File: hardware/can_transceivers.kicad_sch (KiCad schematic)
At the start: 0 parts

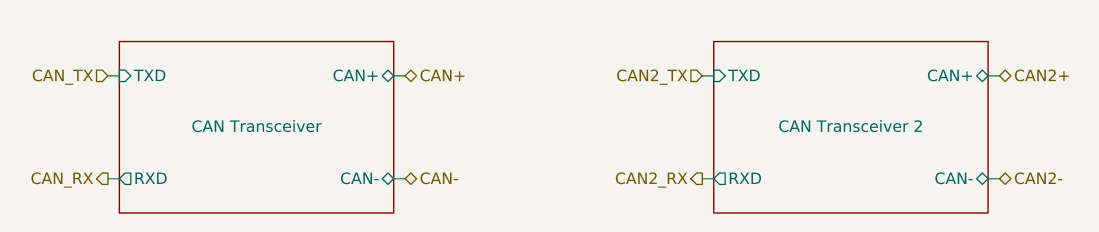
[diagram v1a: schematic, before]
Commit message: Improve the diagram based on the feedback
- add an input LC filter
- remove the USB connector
- add a programmer connector
- move optocouplers into a subsheet
- add a suspension tension meter IC
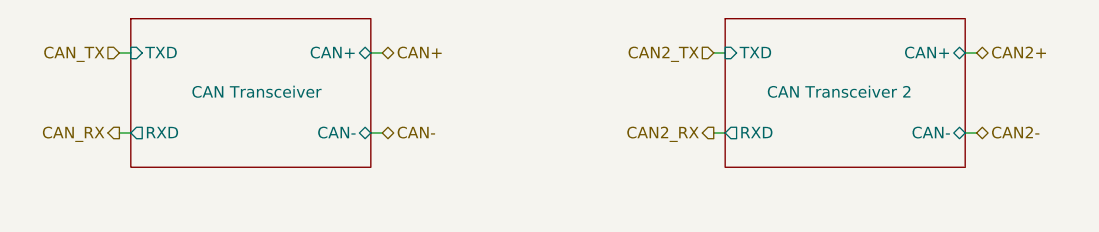
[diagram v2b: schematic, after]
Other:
- title: (none) -> CAN Transceivers
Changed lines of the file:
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@@
   (paper "A4")
   (title_block
-    (date "2023-09-20")
+    (title "CAN Transceivers")
+    (date "2023-10-01")
     (rev "${REVISION}")
     (company "Author: I. Kajdan")
     (comment 1 "Reviewer:")
   )
-  (wire (pts (xy 132.08 106.68) (xy 133.35 106.68))
+  (wire (pts (xy 129.54 101.6) (xy 130.81 101.6))
     (stroke (width 0) (type default))
   )
-  (wire (pts (xy 100.33 106.68) (xy 101.6 106.68))
+  (wire (pts (xy 101.6 101.6) (xy 102.87 101.6))
     (stroke (width 0) (type default))
   )
-  (wire (pts (xy 166.37 95.25) (xy 167.64 95.25))
+  (wire (pts (xy 167.64 92.71) (xy 168.91 92.71))
     (stroke (width 0) (type default))
   )
-  (wire (pts (xy 132.08 95.25) (xy 133.35 95.25))
+  (wire (pts (xy 129.54 92.71) (xy 130.81 92.71))
     (stroke (width 0) (type default))
   )
-  (wire (pts (xy 166.37 106.68) (xy 167.64 106.68))
+  (wire (pts (xy 167.64 101.6) (xy 168.91 101.6))
     (stroke (width 0) (type default))
   )
-  (wire (pts (xy 100.33 95.25) (xy 101.6 95.25))
+  (wire (pts (xy 101.6 92.71) (xy 102.87 92.71))
     (stroke (width 0) (type default))
   )
-  (wire (pts (xy 198.12 95.25) (xy 199.39 95.25))
+  (wire (pts (xy 195.58 92.71) (xy 196.85 92.71))
     (stroke (width 0) (type default))
   )
-  (wire (pts (xy 198.12 106.68) (xy 199.39 106.68))
+  (wire (pts (xy 195.58 101.6) (xy 196.85 101.6))
     (stroke (width 0) (type default))
   )
-  (hierarchical_label "CAN2_RX" (shape output) (at 166.37 106.68 180) (fields_autoplaced)
+  (hierarchical_label "CAN2_RX" (shape output) (at 167.64 101.6 180) (fields_autoplaced)
     (effects (font (size 1.27 1.27)) (justify right))
   )
-  (hierarchical_label "CAN2+" (shape bidirectional) (at 199.39 95.25 0) (fields_autoplaced)
+  (hierarchical_label "CAN2+" (shape bidirectional) (at 196.85 92.71 0) (fields_autoplaced)
     (effects (font (size 1.27 1.27)) (justify left))
   )
-  (hierarchical_label "CAN-" (shape bidirectional) (at 133.35 106.68 0) (fields_autoplaced)
+  (hierarchical_label "CAN-" (shape bidirectional) (at 130.81 101.6 0) (fields_autoplaced)
     (effects (font (size 1.27 1.27)) (justify left))
   )
-  (hierarchical_label "CAN2-" (shape bidirectional) (at 199.39 106.68 0) (fields_autoplaced)
+  (hierarchical_label "CAN2-" (shape bidirectional) (at 196.85 101.6 0) (fields_autoplaced)
     (effects (font (size 1.27 1.27)) (justify left))
   )
-  (hierarchical_label "CAN_RX" (shape output) (at 100.33 106.68 180) (fields_autoplaced)
+  (hierarchical_label "CAN_RX" (shape output) (at 101.6 101.6 180) (fields_autoplaced)
     (effects (font (size 1.27 1.27)) (justify right))
   )
-  (hierarchical_label "CAN2_TX" (shape input) (at 166.37 95.25 180) (fields_autoplaced)
+  (hierarchical_label "CAN2_TX" (shape input) (at 167.64 92.71 180) (fields_autoplaced)
     (effects (font (size 1.27 1.27)) (justify right))
   )
-  (hierarchical_label "CAN_TX" (shape input) (at 100.33 95.25 180) (fields_autoplaced)
+  (hierarchical_label "CAN_TX" (shape input) (at 101.6 92.71 180) (fields_autoplaced)
     (effects (font (size 1.27 1.27)) (justify right))
   )
-  (hierarchical_label "CAN+" (shape bidirectional) (at 133.35 95.25 0) (fields_autoplaced)
+  (hierarchical_label "CAN+" (shape bidirectional) (at 130.81 92.71 0) (fields_autoplaced)
     (effects (font (size 1.27 1.27)) (justify left))
   )
-  (sheet (at 101.6 91.44) (size 30.48 19.05)
+  (sheet (at 102.87 88.9) (size 26.67 16.51)
     (stroke (width 0.1524) (type solid))
     (fill (color 0 0 0 0.0000))
-    (property "Sheetname" "CAN Transceiver" (at 116.84 100.8884 0)
+    (property "Sheetname" "CAN Transceiver" (at 116.84 97.0784 0)
       (effects (font (size 1.27 1.27)))
     )
-    (property "Sheetfile" "can_transceiver.kicad_sch" (at 101.6 108.5346 0)
+    (property "Sheetfile" "can_transceiver.kicad_sch" (at 102.87 105.9946 0)
       (effects (font (size 1.27 1.27)) (justify left top) hide)
     )
-    (pin "RXD" output (at 101.6 106.68 180)
+    (pin "RXD" output (at 102.87 101.6 180)
       (effects (font (size 1.27 1.27)) (justify left))
     )
-    (pin "TXD" input (at 101.6 95.25 180)
+    (pin "TXD" input (at 102.87 92.71 180)
       (effects (font (size 1.27 1.27)) (justify left))
     )
-    (pin "CAN-" bidirectional (at 132.08 106.68 0)
+    (pin "CAN-" bidirectional (at 129.54 101.6 0)
       (effects (font (size 1.27 1.27)) (justify right))
     )
-    (pin "CAN+" bidirectional (at 132.08 95.25 0)
+    (pin "CAN+" bidirectional (at 129.54 92.71 0)
       (effects (font (size 1.27 1.27)) (justify right))
     )
@@
       (project "rearbox"
         (path "/b652b05a-4e3d-4ad1-b032-18886abe7d45" (page "8"))
-        (path "/b652b05a-4e3d-4ad1-b032-18886abe7d45/38408e41-dfb1-4c27-acb0-3f1224cc8789" (page "6"))
+        (path "/b652b05a-4e3d-4ad1-b032-18886abe7d45/38408e41-dfb1-4c27-acb0-3f1224cc8789" (page "5"))
       )
     )
   )
-  (sheet (at 167.64 91.44) (size 30.48 19.05)
+  (sheet (at 168.91 88.9) (size 26.67 16.51)
     (stroke (width 0.1524) (type solid))
     (fill (color 0 0 0 0.0000))
-    (property "Sheetname" "CAN Transceiver 2" (at 182.88 100.8884 0)
+    (property "Sheetname" "CAN Transceiver 2" (at 181.61 97.0784 0)
       (effects (font (size 1.27 1.27)))
     )
-    (property "Sheetfile" "can_transceiver.kicad_sch" (at 167.64 108.5346 0)
+    (property "Sheetfile" "can_transceiver.kicad_sch" (at 168.91 105.9946 0)
       (effects (font (size 1.27 1.27)) (justify left top) hide)
     )
-    (pin "RXD" output (at 167.64 106.68 180)
+    (pin "RXD" output (at 168.91 101.6 180)
       (effects (font (size 1.27 1.27)) (justify left))
     )
-    (pin "TXD" input (at 167.64 95.25 180)
+    (pin "TXD" input (at 168.91 92.71 180)
       (effects (font (size 1.27 1.27)) (justify left))
     )
-    (pin "CAN-" bidirectional (at 198.12 106.68 0)
+    (pin "CAN-" bidirectional (at 195.58 101.6 0)
       (effects (font (size 1.27 1.27)) (justify right))
     )
-    (pin "CAN+" bidirectional (at 198.12 95.25 0)
+    (pin "CAN+" bidirectional (at 195.58 92.71 0)
       (effects (font (size 1.27 1.27)) (justify right))
     )
@@
       (project "rearbox"
         (path "/b652b05a-4e3d-4ad1-b032-18886abe7d45" (page "9"))
-        (path "/b652b05a-4e3d-4ad1-b032-18886abe7d45/38408e41-dfb1-4c27-acb0-3f1224cc8789" (page "7"))
+        (path "/b652b05a-4e3d-4ad1-b032-18886abe7d45/38408e41-dfb1-4c27-acb0-3f1224cc8789" (page "6"))
       )
     )
